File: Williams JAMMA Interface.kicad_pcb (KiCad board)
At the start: 2 copper layers, 112.2 x 74.8 mm, 39 parts, among them P1 10K, U1 LM386, U2 DIP-14_W7.62mm_Socket, U3 MC34063AP

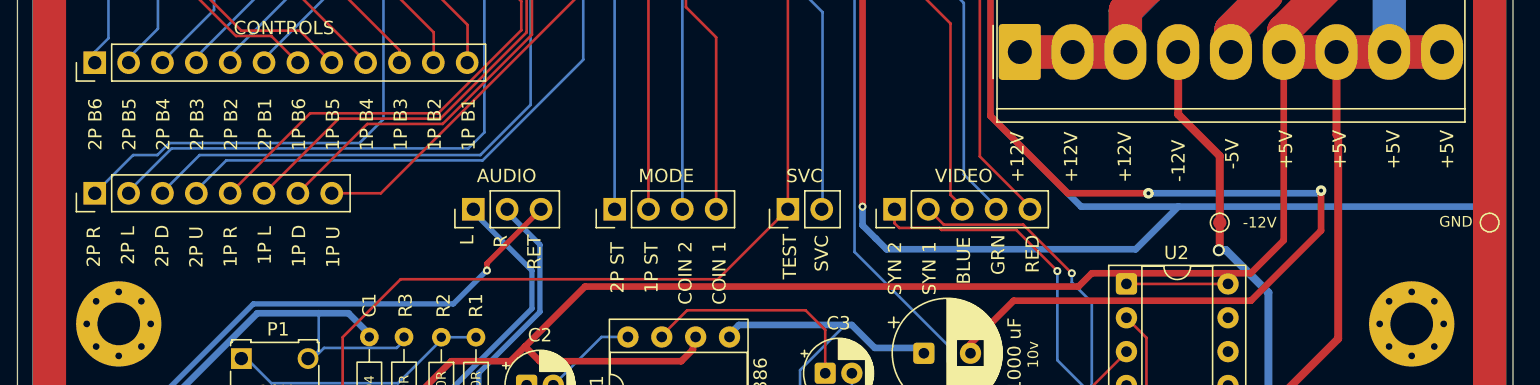
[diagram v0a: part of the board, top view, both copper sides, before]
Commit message: silkscreen alignment
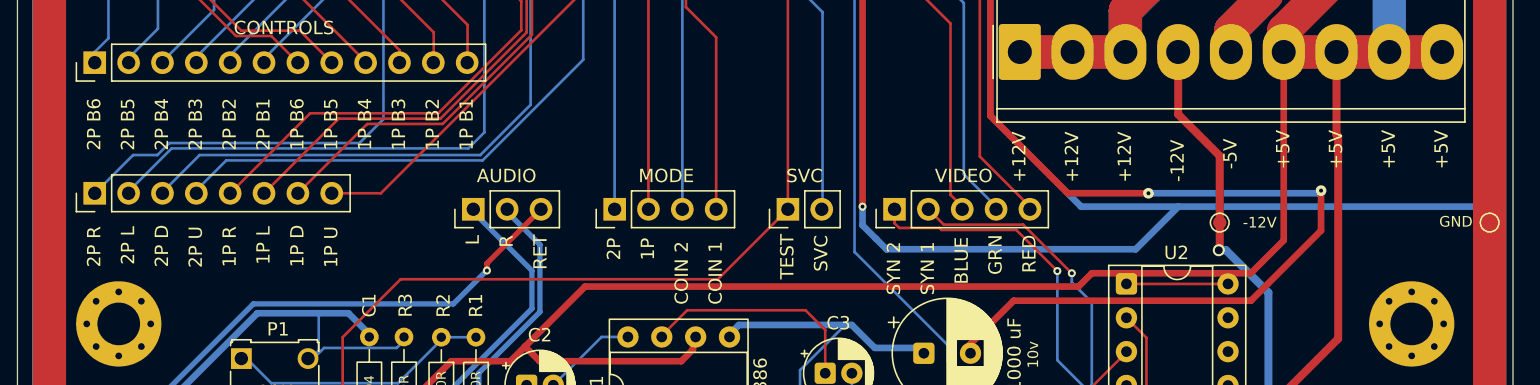
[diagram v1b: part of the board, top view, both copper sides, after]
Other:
- board text added: "1P"
- board text added: "2P"
- board text removed: "1P ST"
- board text removed: "2P ST"
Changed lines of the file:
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@@
 	)
 	(gr_text "SYN 2"
-		(at 159.820303 102.652734 90)
+		(at 159.7395 102.652734 90)
 		(layer "F.SilkS")
 		(effects
@@
 	)
 	(gr_text "L"
-		(at 127.720225 98.890829 90)
+		(at 128.1395 98.890829 90)
 		(layer "F.SilkS")
 		(effects
@@
 	)
 	(gr_text "+5V"
-		(at 193.177046 93.2 90)
-		(layer "F.SilkS")
-		(effects
-			(font
-				(size 1 1)
-				(thickness 0.1)
-			)
-			(justify left bottom)
-		)
-	)
-	(gr_text "2P ST"
-		(at 138.997851 102.509877 90)
+		(at 192.8995 93.2 90)
+		(layer "F.SilkS")
+		(effects
+			(font
+				(size 1 1)
+				(thickness 0.1)
+			)
+			(justify left bottom)
+		)
+	)
+	(gr_text "2P"
+		(at 138.7395 100.033686 90)
 		(layer "F.SilkS")
 		(effects
@@
 	)
 	(gr_text "GRN"
-		(at 167.563083 101.128924 90)
+		(at 167.3595 101.128924 90)
 		(layer "F.SilkS")
 		(effects
@@
 	)
 	(gr_text "1P B5"
-		(at 117.646431 91.8 90)
+		(at 117.5195 91.8 90)
 		(layer "F.SilkS")
 		(effects
@@
 	)
 	(gr_text "2P B5"
-		(at 102.373704 91.8 90)
+		(at 102.2795 91.8 90)
 		(layer "F.SilkS")
 		(effects
@@
 	)
 	(gr_text "SVC"
-		(at 154.325819 100.890829 90)
+		(at 154.2795 100.890829 90)
 		(layer "F.SilkS")
 		(effects
@@
 	)
 	(gr_text "2P B4"
-		(at 104.919158 91.8 90)
+		(at 104.8195 91.8 90)
 		(layer "F.SilkS")
 		(effects
@@
 	)
 	(gr_text "+12V"
-		(at 169 94.2 90)
+		(at 169.1395 94.2 90)
 		(layer "F.SilkS")
 		(effects
@@
 	)
 	(gr_text "BLUE"
-		(at 164.982156 101.84321 90)
+		(at 164.8195 101.84321 90)
 		(layer "F.SilkS")
 		(effects
@@
 	)
 	(gr_text "+12V"
-		(at 173.029508 94.2 90)
+		(at 173.0995 94.2 90)
 		(layer "F.SilkS")
 		(effects
@@
 	)
 	(gr_text "2P B2"
-		(at 110.010067 91.8 90)
+		(at 109.8995 91.8 90)
 		(layer "F.SilkS")
 		(effects
@@
 	)
 	(gr_text "+5V"
-		(at 201.236061 93.2 90)
+		(at 200.8195 93.2 90)
 		(layer "F.SilkS")
 		(effects
@@
 	)
 	(gr_text "1P U"
-		(at 117.669816 100.6 90)
+		(at 117.5195 100.6 90)
 		(layer "F.SilkS")
 		(effects
@@
 	)
 	(gr_text "1P B4"
-		(at 120.191885 91.8 90)
+		(at 120.0595 91.8 90)
 		(layer "F.SilkS")
 		(effects
@@
 	)
 	(gr_text "2P B3"
-		(at 107.464613 91.8 90)
+		(at 107.3595 91.8 90)
 		(layer "F.SilkS")
 		(effects
@@
 	)
 	(gr_text "-5V"
-		(at 185.118031 93.2 90)
+		(at 184.9795 93.2 90)
 		(layer "F.SilkS")
 		(effects
@@
 	)
 	(gr_text "+5V"
-		(at 197.206553 93.2 90)
+		(at 196.8595 93.2 90)
 		(layer "F.SilkS")
 		(effects
@@
 	)
 	(gr_text "1P D"
-		(at 115.104317 100.552381 90)
+		(at 114.9795 100.552381 90)
 		(layer "F.SilkS")
 		(effects
@@
 	)
 	(gr_text "SYN 1"
-		(at 162.40123 102.652734 90)
+		(at 162.2795 102.652734 90)
 		(layer "F.SilkS")
 		(effects
@@
 	)
 	(gr_text "RED"
-		(at 170.144009 100.986067 90)
+		(at 169.8995 100.986067 90)
 		(layer "F.SilkS")
 		(effects
@@
 	)
 	(gr_text "TEST"
-		(at 151.930774 101.462258 90)
+		(at 151.7395 101.462258 90)
 		(layer "F.SilkS")
 		(effects
@@
 	)
 	(gr_text "1P B3"
-		(at 122.73734 91.8 90)
+		(at 122.5995 91.8 90)
 		(layer "F.SilkS")
 		(effects
@@
 	)
 	(gr_text "RET"
-		(at 132.760843 100.747972 90)
+		(at 133.2195 100.747972 90)
 		(layer "F.SilkS")
 		(effects
@@
 	)
 	(gr_text "2P L"
-		(at 102.276823 100.361905 90)
+		(at 102.2795 100.361905 90)
 		(layer "F.SilkS")
 		(effects
@@
 	)
 	(gr_text "2P U"
-		(at 107.407821 100.6 90)
-		(layer "F.SilkS")
-		(effects
-			(font
-				(size 1 1)
-				(thickness 0.1)
-			)
-			(justify left bottom)
-		)
-	)
-	(gr_text "1P ST"
-		(at 141.547129 102.509877 90)
+		(at 107.3595 100.6 90)
+		(layer "F.SilkS")
+		(effects
+			(font
+				(size 1 1)
+				(thickness 0.1)
+			)
+			(justify left bottom)
+		)
+	)
+	(gr_text "1P"
+		(at 141.2795 100.033686 90)
 		(layer "F.SilkS")
 		(effects
@@
 	)
 	(gr_text "+12V"
-		(at 177.059015 94.2 90)
+		(at 177.0595 94.2 90)
 		(layer "F.SilkS")
 		(effects
@@
 	)
 	(gr_text "2P B1"
-		(at 112.555522 91.8 90)
+		(at 112.4395 91.8 90)
 		(layer "F.SilkS")
 		(effects
@@
 	)
 	(gr_text "1P B1"
-		(at 127.828249 91.8 90)
+		(at 127.6795 91.8 90)
 		(layer "F.SilkS")
 		(effects
@@
 	)
 	(gr_text "2P B6"
-		(at 99.828249 91.8 90)
+		(at 99.7395 91.8 90)
 		(layer "F.SilkS")
 		(effects
@@
 	)
 	(gr_text "COIN 2"
-		(at 144.096406 103.367019 90)
+		(at 143.8195 103.367019 90)
 		(layer "F.SilkS")
 		(effects
@@
 	)
 	(gr_text "1P L"
-		(at 112.538818 100.361905 90)
+		(at 112.4395 100.361905 90)
 		(layer "F.SilkS")
 		(effects
@@
 	)
 	(gr_text "COIN 1"
-		(at 146.645684 103.367019 90)
+		(at 146.3595 103.367019 90)
 		(layer "F.SilkS")
 		(effects
@@
 	)
 	(gr_text "+5V"
-		(at 189.147538 93.2 90)
+		(at 188.9395 93.2 90)
 		(layer "F.SilkS")
 		(effects
@@
 	)
 	(gr_text "R"
-		(at 130.240534 99.081305 90)
+		(at 130.6795 99.081305 90)
 		(layer "F.SilkS")
 		(effects
@@
 	)
 	(gr_text "2P D"
-		(at 104.842322 100.552381 90)
+		(at 104.8195 100.552381 90)
 		(layer "F.SilkS")
 		(effects
@@
 	)
 	(gr_text "1P R"
-		(at 109.973319 100.552381 90)
+		(at 109.8995 100.552381 90)
 		(layer "F.SilkS")
 		(effects
@@
 	)
 	(gr_text "-12V"
-		(at 181.088523 94.152381 90)
+		(at 181.0195 94.152381 90)
 		(layer "F.SilkS")
 		(effects
@@
 	)
 	(gr_text "1P B2"
-		(at 125.282794 91.8 90)
+		(at 125.1395 91.8 90)
 		(layer "F.SilkS")
 		(effects
@@
 	)
 	(gr_text "1P B6"
-		(at 115.100976 91.8 90)
+		(at 114.9795 91.8 90)
 		(layer "F.SilkS")
 		(effects
@@
 	)
 	(gr_text "2P R"
-		(at 99.711324 100.552381 90)
-		(layer "F.SilkS")
-		(effects
+		(at 99.7395 100.552381 90)
+		(layer "F.SilkS")
+		(effects

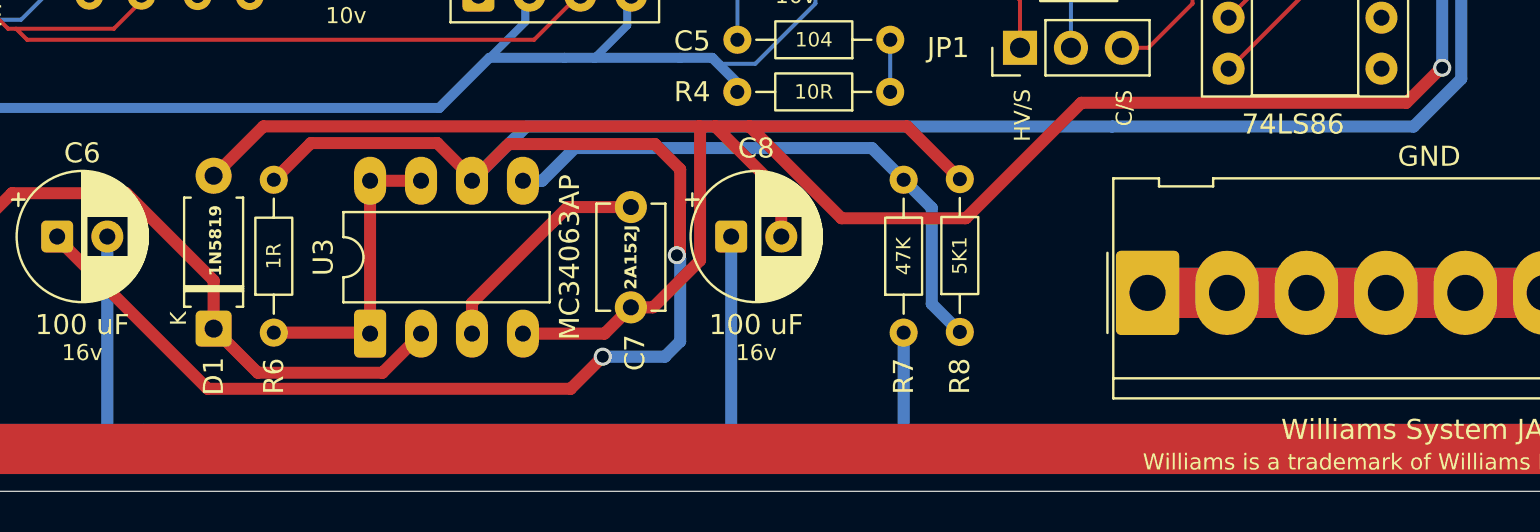
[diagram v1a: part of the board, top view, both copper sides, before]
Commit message: 3.4mm film caps for 152
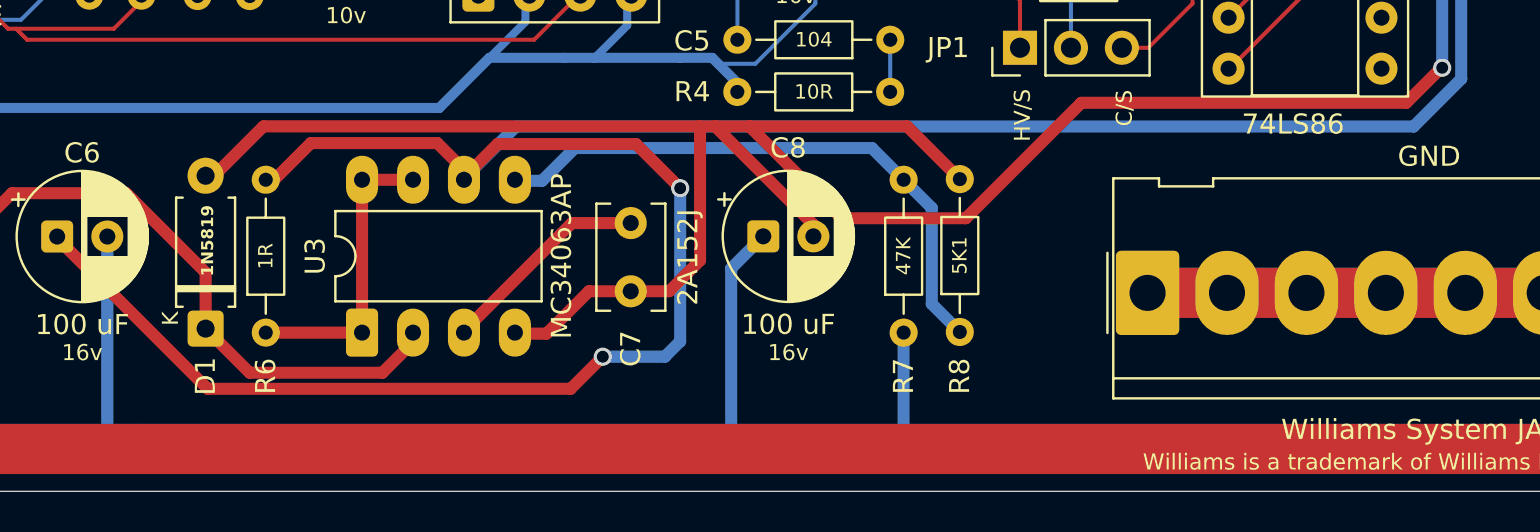
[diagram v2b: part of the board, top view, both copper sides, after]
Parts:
- C7: footprint Capacitor_THT:C_Disc_D5.1mm_W3.2mm_P5.00mm -> Capacitor_THT:C_Disc_D5.1mm_W3.2mm_P3.4mm
- moved C8 1.60 mm to (153.4, 125.4)
- moved U3 0.40 mm to (133.4, 130.2)
- moved D1 0.40 mm to (125.6, 130.0)
- moved R6 0.40 mm to (128.6, 130.2)
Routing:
- net -12V: track 138.5 -> 140.0 mm
- net U3_CAP: track 11.4 -> 10.6 mm
- net GND: track 909.5 -> 910.2 mm
